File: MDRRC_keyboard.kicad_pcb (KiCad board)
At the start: 2 copper layers, 16 parts, among them CON1 AVR-ISP-6, IC1 ATMEGA8-AI, P1 LCD, P2 CONN_8, P3 CONN_4

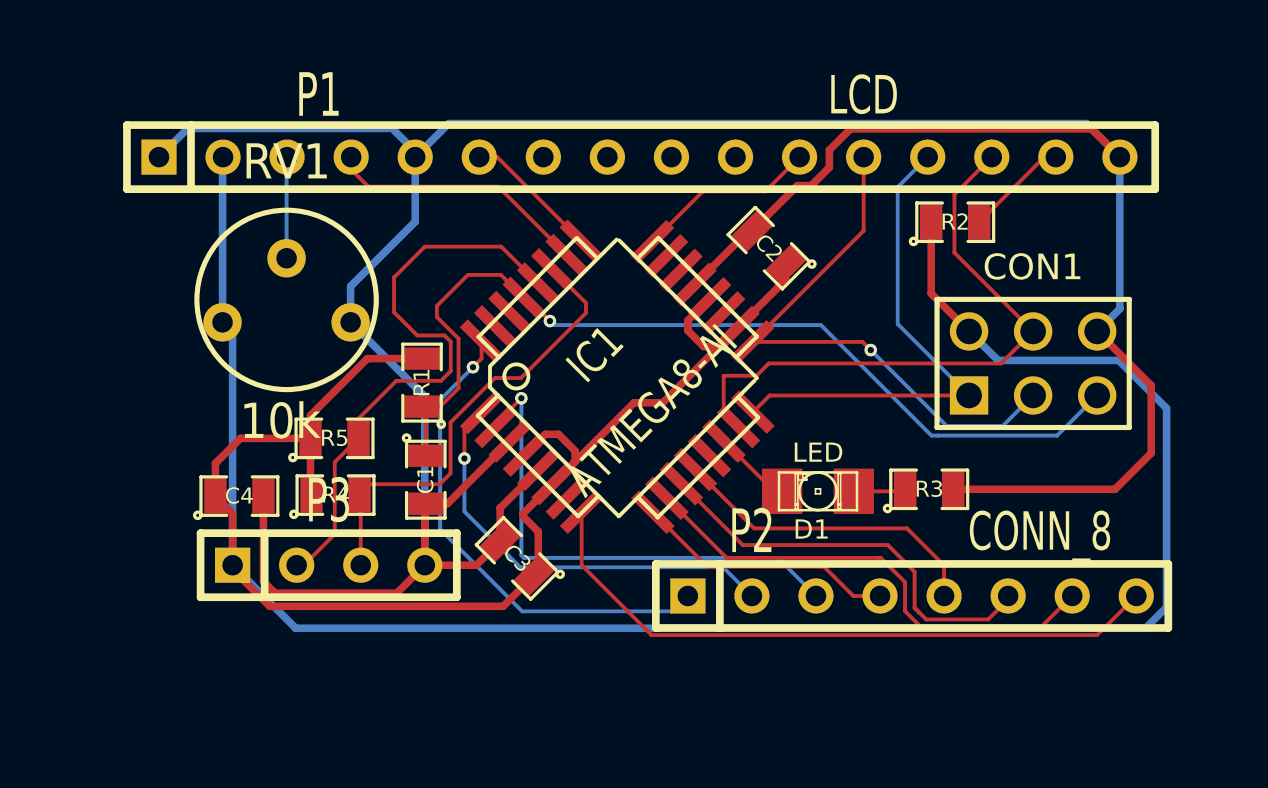
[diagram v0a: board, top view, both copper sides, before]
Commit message: Updated board to include previous changes to schematic
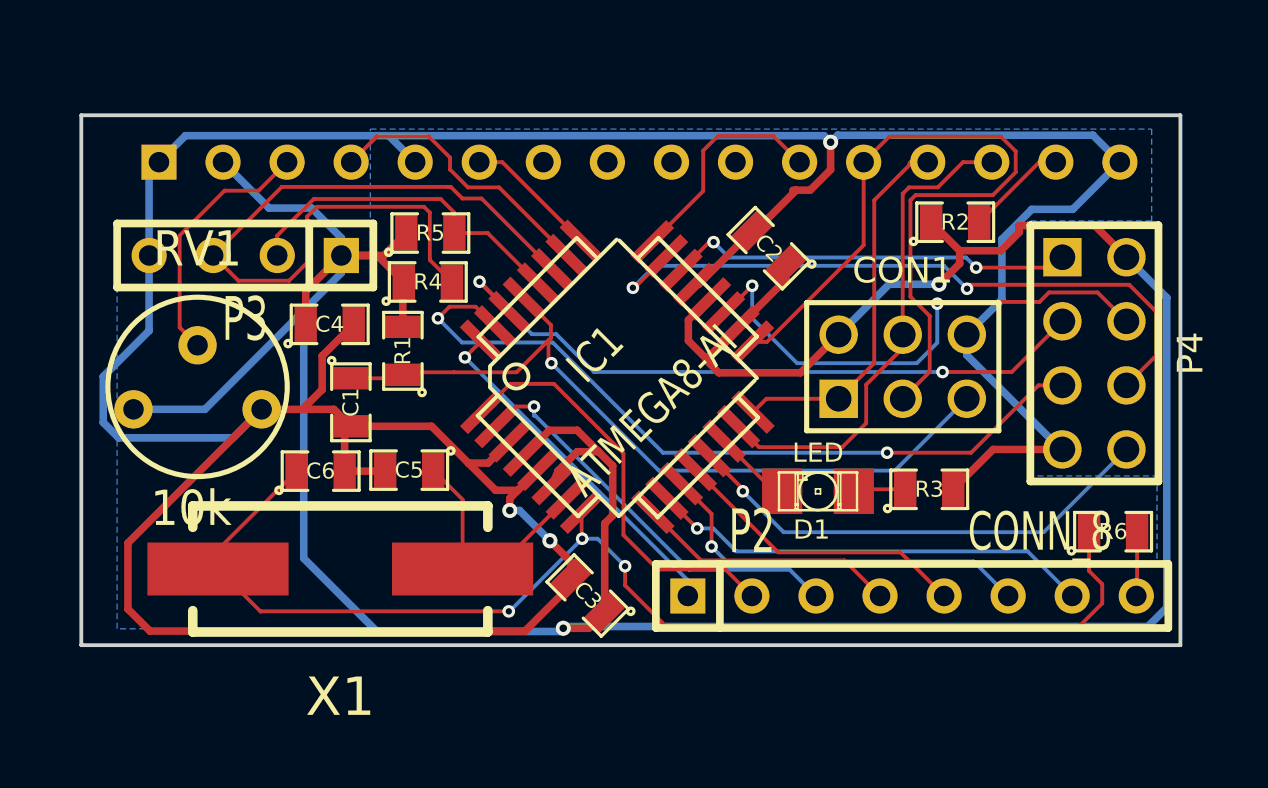
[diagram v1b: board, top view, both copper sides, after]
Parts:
- added C5: C, SM0805, F.Cu at (151.1, 80.8)
- added C6: C, SM0805, F.Cu at (147.6, 80.9)
- added P4: CONN_4X2, pin_array_4x2, F.Cu at (178.3, 76.2)
- added R6: 0, SM0805, F.Cu at (179.0, 83.3)
- added X1: CRYSTAL, Crystal_HC49-SD_SMD_RevA_09Aug2010, F.Cu at (148.4, 84.8)
- P1: moved to B.Cu
- moved P3 12.7 mm to (144.6, 72.3), turned to 180 degrees
- moved R4 9.21 mm to (151.9, 73.4)
- moved R5 8.98 mm to (152.0, 71.5)
- moved C4 7.69 mm to (148.0, 75.1)
- moved CON1 5.17 mm to (170.7, 76.8)
- moved RV1 4.94 mm to (142.7, 77.2)
- moved C1 4.27 mm to (148.8, 78.2)
- moved C3 3.16 mm to (158.2, 85.8)
- moved R1 1.47 mm to (150.9, 76.1)
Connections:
- IC1 pad 13: (no net) -> PB1
- IC1 pad 19: (no net) -> N-0000016
- IC1 pad 22: (no net) -> N-0000017
- IC1 pad 23: (no net) -> PC0
- IC1 pad 30: (no net) -> N-0000010
- IC1 pad 31: (no net) -> N-0000011
- IC1 pad 7: (no net) -> N-000008
- IC1 pad 8: N-0000019 (its old number) -> N-000007
- P2 pad 8: N-0000019 (its old number) -> N-000001
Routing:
- net N-000007: track 0.00 -> 48.5 mm, vias 0 -> 3
- net N-0000011: track 0.00 -> 30.9 mm, vias 0 -> 2
- net PC0: track 0.00 -> 27.3 mm, vias 0 -> 2
- net N-0000010: track 0.00 -> 27.2 mm, vias 0 -> 2
- net N-0000019 (its old number): track 25.9 -> 0.00 mm
- net N-0000016: track 0.00 -> 21.0 mm, vias 0 -> 2
- net GND: track 124.6 -> 144.6 mm, vias 0 -> 3
- net PB1: track 0.00 -> 19.2 mm, vias 0 -> 1
- net N-0000017: track 0.00 -> 16.2 mm, vias 0 -> 2
- net /SDA: track 18.2 -> 30.5 mm
- net /SCL: track 23.6 -> 13.6 mm
- net N-000008: track 0.00 -> 9.72 mm
- net SCK: track 22.2 -> 30.1 mm, vias 1 -> 0
- net N-0000035: track 37.4 -> 31.0 mm
- net N-0000022: track 4.02 -> 10.1 mm
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- added copper zone on B.Cu, net GND
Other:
- board outline added: 43.6 x 21 mm

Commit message: Silkscreen update, rev 0
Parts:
- added ?: , dp_devices-CC-BY-SA, B.Cu at (154.9, 86.9)
- P2: value CONN_8 -> Keyboard
- renumbered CON1 to AVR, RV1 to Contrast
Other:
- board text added: "3. PD0 4. ADC6 5. PD1"
- board text added: "6. PC0 7. GND 8. PB1"
- board text added: "MDRRC Keyboard rev. 0"
- board text added: "Original schematic: Robert Everts Extended by, Board by: Dirkjan Krijnders"
- board text added: "P1: 1. Vcc 2. SCL 3. SDA 4. GND"
- board text added: "P4: 1. ADC7 2. Vcc"
- board text added: "https://github.com/dirkjankrijnders/MDRRC-Keyboard"
